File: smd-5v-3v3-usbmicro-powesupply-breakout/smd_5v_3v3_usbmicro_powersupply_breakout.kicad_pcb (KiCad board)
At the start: 2 copper layers, 32 x 40 mm, 11 parts, among them J1 USB_B_Micro, J2 SMD Pads, J3 THT Pins, U1 LMS1585AIS-3.3

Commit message: All pcb traces/connections set
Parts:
- moved C2 0.28 mm to (154.8, 112.4)
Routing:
- net +5V: track 0.00 -> 33.7 mm
- net +3V3: track 0.00 -> 30.7 mm
- net VBUS: track 0.00 -> 9.36 mm
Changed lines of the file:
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@@
 	(footprint "Capacitor_SMD:C_0603_1608Metric"
 		(layer "F.Cu")
-		(at 155 112.225 90)
+		(at 154.8 112.425 90)
 		(descr "Capacitor SMD 0603 (1608 Metric), square (rectangular) end terminal, IPC_7351 nominal, (Body size source: IPC-SM-782 page 76, https://www.pcb-3d.com/wordpress/wp-content/uploads/ipc-sm-782a_amendment_1_and_2.pdf), generated with kicad-footprint-generator")
 		(tags "capacitor")
@@
 		(layer "Edge.Cuts")
 	)
+	(segment
+		(start 158.7 133.6)
+		(end 159.3 133)
+		(width 0.5)
+		(layer "F.Cu")
+		(net 1)
+	)
+	(segment
+		(start 159.3 133)
+		(end 159.3 129.9375)
+		(width 0.5)
+		(layer "F.Cu")
+		(net 1)
+	)
+	(segment
+		(start 159.3 129.9375)
+		(end 157 127.6375)
+		(width 0.5)
+		(layer "F.Cu")
+		(net 1)
+	)
+	(segment
+		(start 158.7 135.8)
+		(end 158.7 133.6)
+		(width 0.5)
+		(layer "F.Cu")
+		(net 1)
+	)
+	(segment
+		(start 159 120.3625)
+		(end 159 119)
+		(width 0.8)
+		(layer "F.Cu")
+		(net 3)
+	)
+	(segment
+		(start 157 122.3625)
+		(end 159 120.3625)
+		(width 0.8)
+		(layer "F.Cu")
+		(net 3)
+	)
+	(segment
+		(start 158 107)
+		(end 157 107)
+		(width 0.7)
+		(layer "F.Cu")
+		(net 3)
+	)
+	(segment
+		(start 157 117)
+		(end 154.8 117)
+		(width 0.8)
+		(layer "F.Cu")
+		(net 3)
+	)
+	(segment
+		(start 157 103.125)
+		(end 158 102.125)
+		(width 0.7)
+		(layer "F.Cu")
+		(net 3)
+	)
+	(segment
+		(start 157 107)
+		(end 155 109)
+		(width 0.7)
+		(layer "F.Cu")
+		(net 3)
+	)
+	(segment
+		(start 154.8 117)
+		(end 154.8 113.8)
+		(width 0.8)
+		(layer "F.Cu")
+		(net 3)
+	)
+	(segment
+		(start 158 107)
+		(end 157 106)
+		(width 0.7)
+		(layer "F.Cu")
+		(net 3)
+	)
+	(segment
+		(start 157 106)
+		(end 157 103.125)
+		(width 0.7)
+		(layer "F.Cu")
+		(net 3)
+	)
+	(segment
+		(start 155 109)
+		(end 150 109)
+		(width 0.7)
+		(layer "F.Cu")
+		(net 3)
+	)
+	(segment
+		(start 159 119)
+		(end 157 117)
+		(width 0.8)
+		(layer "F.Cu")
+		(net 3)
+	)
+	(segment
+		(start 154.8 113.8)
+		(end 150 109)
+		(width 0.8)
+		(layer "F.Cu")
+		(net 3)
+	)
+	(segment
+		(start 161 103.125)
+		(end 160 102.125)
+		(width 0.7)
+		(layer "F.Cu")
+		(net 4)
+	)
+	(segment
+		(start 171 109)
+		(end 169 107)
+		(width 0.8)
+		(layer "F.Cu")
+		(net 4)
+	)
+	(segment
+		(start 171 122.2)
+		(end 171 109)
+		(width 0.8)
+		(layer "F.Cu")
+		(net 4)
+	)
+	(segment
+		(start 160 107)
+		(end 161 106)
+		(width 0.7)
+		(layer "F.Cu")
+		(net 4)
+	)
+	(segment
+		(start 169 107)
+		(end 160.025 107)
+		(width 0.8)
+		(layer "F.Cu")
+		(net 4)
+	)
+	(segment
+		(start 161 106)
+		(end 161 103.125)
+		(width 0.7)
+		(layer "F.Cu")
+		(net 4)
+	)
 	(zone

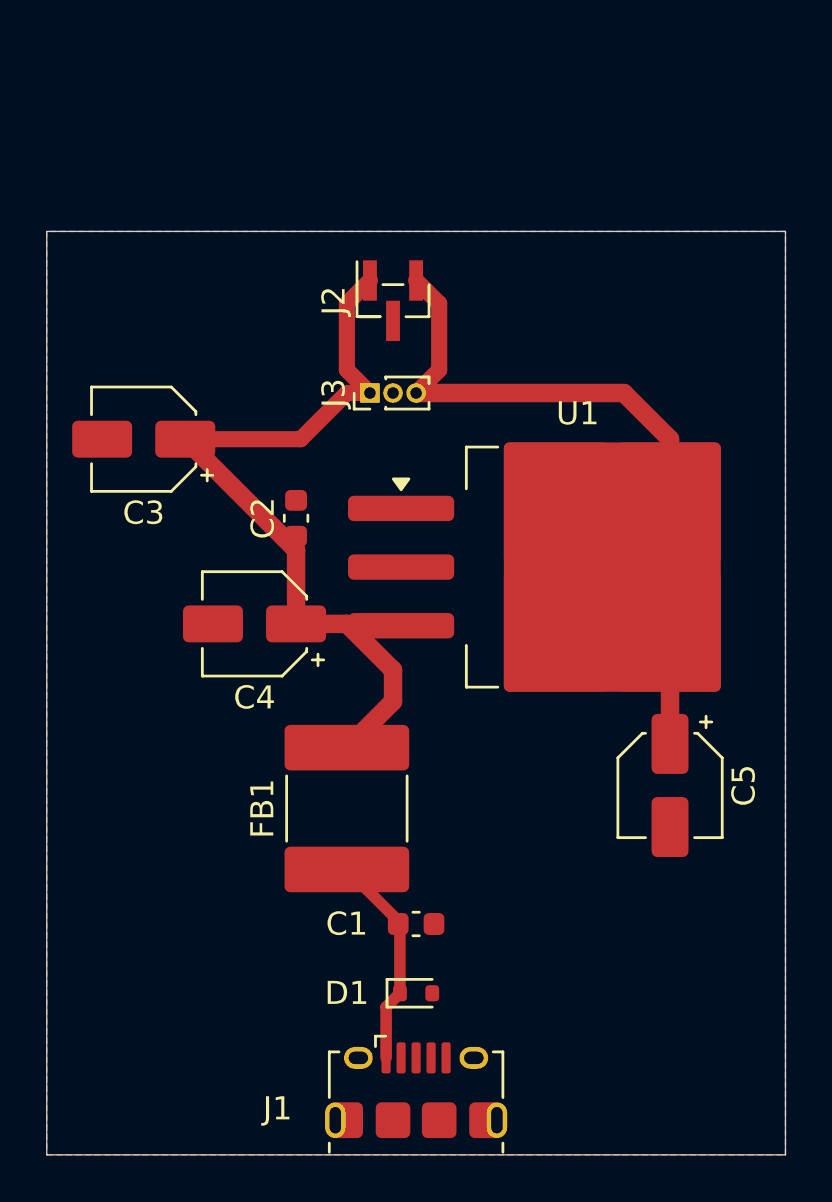
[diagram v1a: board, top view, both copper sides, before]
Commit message: Update schematic and pcb
- Having the 3 pin connectors was awkward, split them up into two
  separate connectors for each power plane
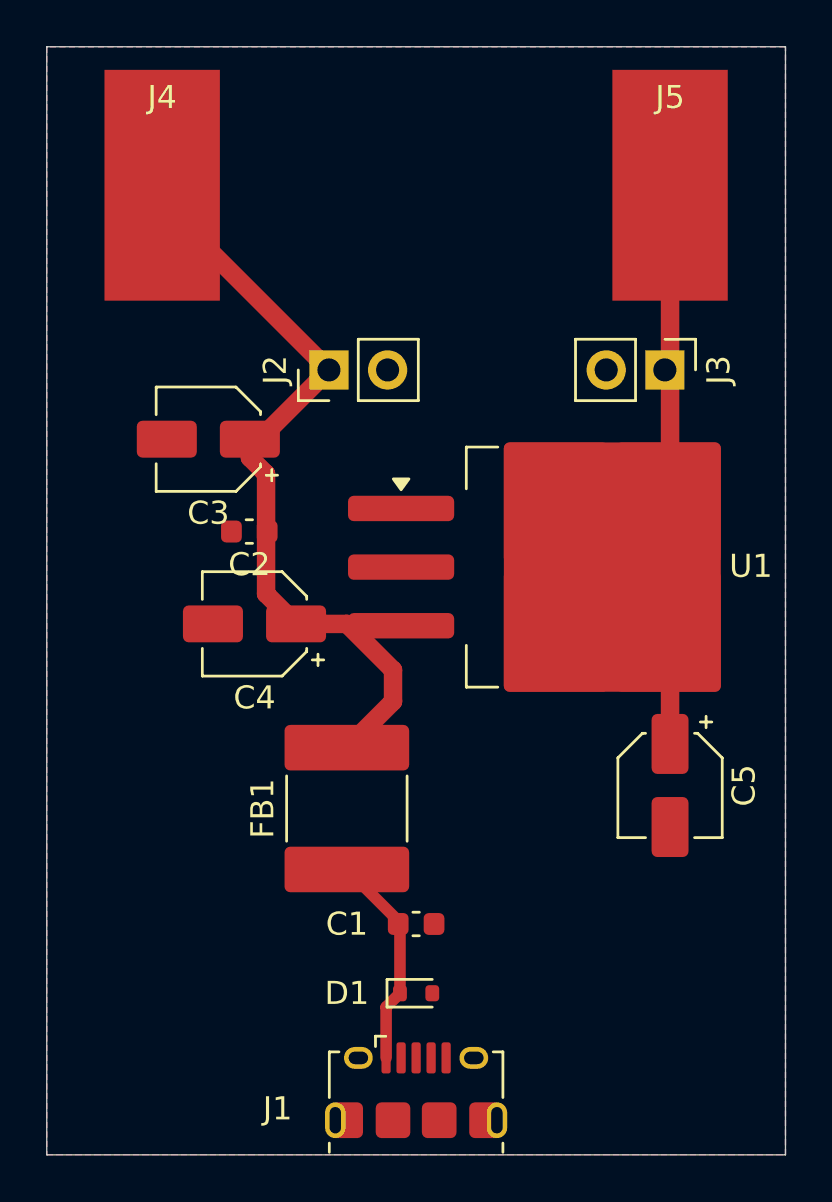
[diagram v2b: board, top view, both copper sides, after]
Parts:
- added J4: SMD 5V Pad, Connector_Wire:SolderWirePad_1x01_SMD_5x10mm, F.Cu at (149.0, 98.0)
- added J5: SMD 3V3 Pad, Connector_Wire:SolderWirePad_1x01_SMD_5x10mm, F.Cu at (171.0, 98.0)
- J2: value SMD Pads -> THT 5V Jumper; footprint Connector_PinHeader_1.00mm:PinHeader_1x03_P1.00mm_Vertical_SMD_Pin1Right -> Connector_PinHeader_2.54mm:PinHeader_1x02_P2.54mm_Vertical
- J3: value THT Pins -> THT 3V3 Jumper; footprint Connector_PinHeader_1.00mm:PinHeader_1x03_P1.00mm_Vertical -> Connector_PinHeader_2.54mm:PinHeader_1x02_P2.54mm_Vertical
- moved J3 12.8 mm to (170.8, 106.0), turned to -90 degrees
- moved J2 4.09 mm to (156.2, 106.0)
- moved C3 2.80 mm to (151.0, 109.0)
- moved C2 2.11 mm to (152.8, 113.0), turned to 180 degrees
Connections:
- J3 pad 1: +5V -> +3V3
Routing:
- net +3V3: track 30.7 -> 24.2 mm
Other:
- board size 32 x 40 mm -> 32 x 48 mm
